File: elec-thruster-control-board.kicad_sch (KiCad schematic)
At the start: 53 parts, among them J1 Conn_01x01, J10 Conn_01x01, J11 gp17-pwm0B, J12 gp2-pwm1A, J14 Conn_01x01, J15 gp6-pwm3A, J16 gp8-pwm4A, J17 Conn_01x01, J18 gp19-pwm1B, J19 gp21-pwm2B, J2 gp0-pwm0A, J20 gp26-pwm5A, J21 gp27-pwm5B, J3 Conn_01x01, J4 Conn_01x01, J5 gp4-pwm2A, J6 Conn_01x01, J7 Conn_01x01, J8 Conn_01x01, J9 Conn_01x01

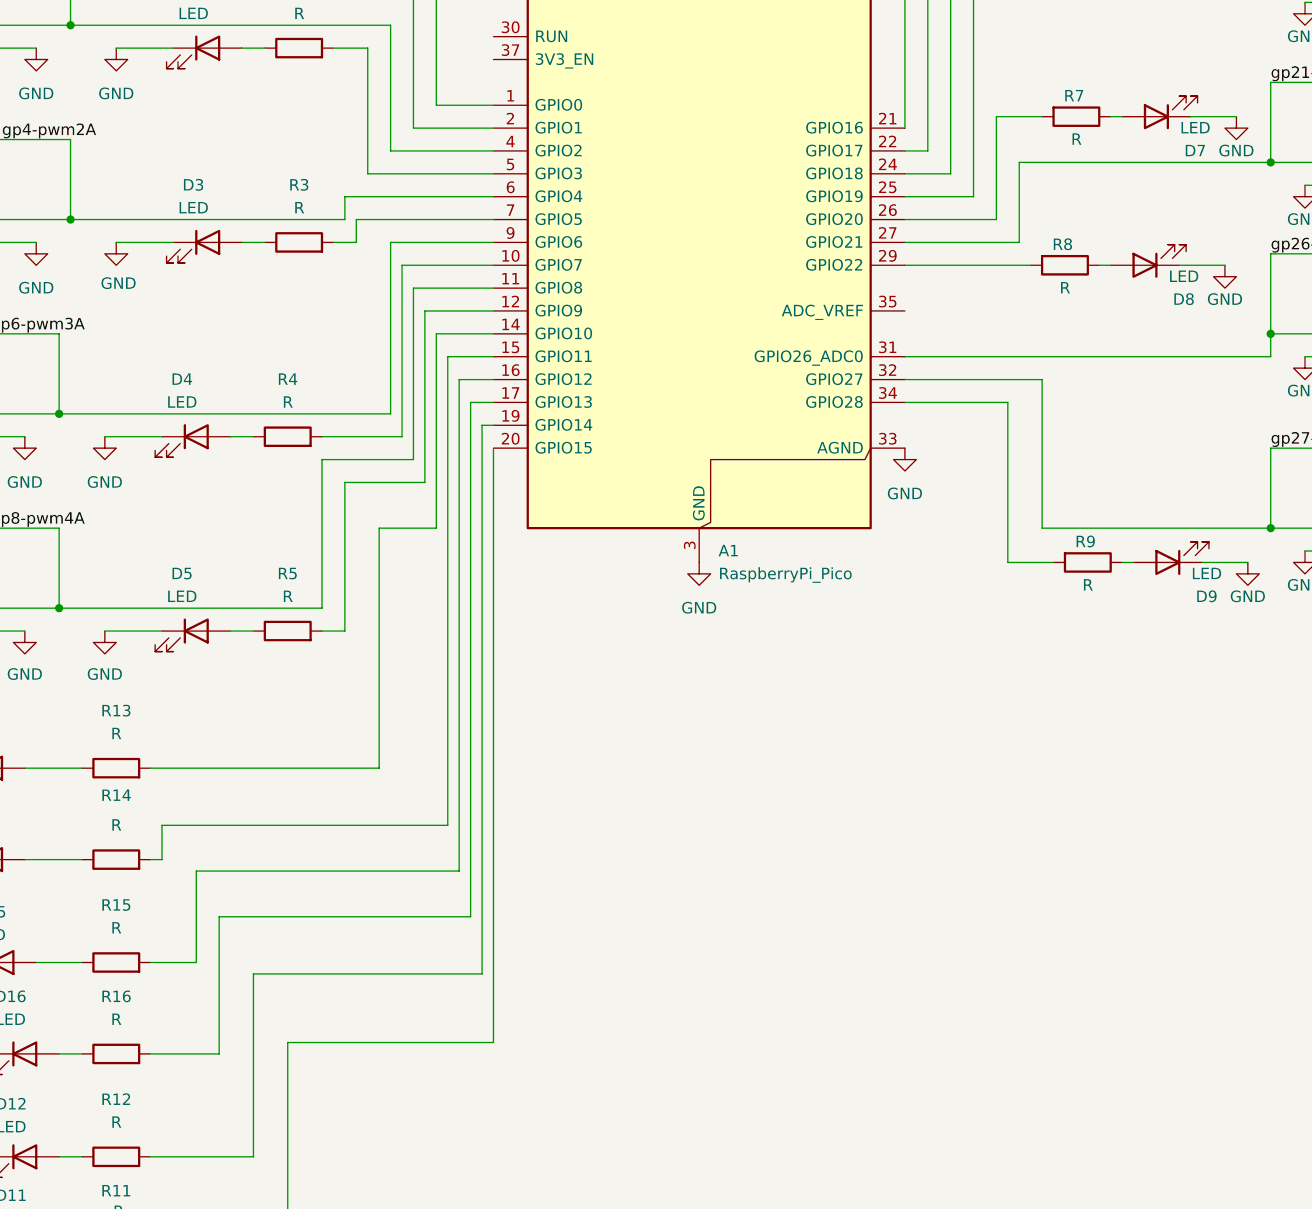
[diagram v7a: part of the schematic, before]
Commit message: Painstakingly added better silkscreening and MOUNTING HOLES!
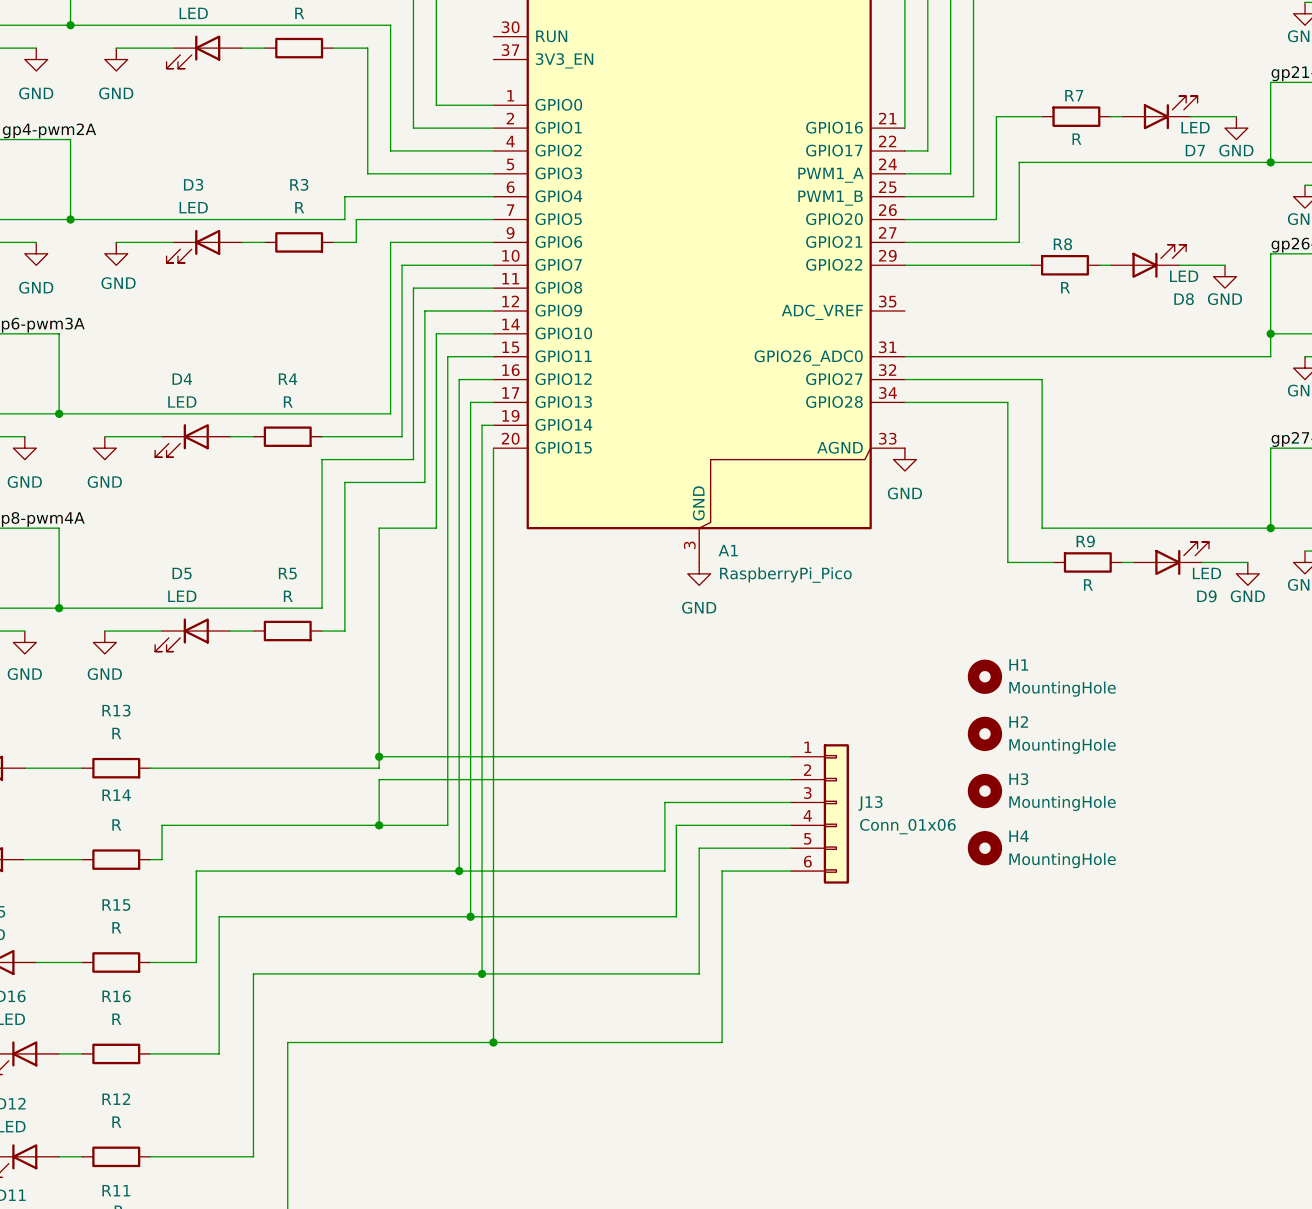
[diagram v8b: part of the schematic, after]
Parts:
- added H1, H2, H3, H4: MountingHole, MountingHole:MountingHole_3.2mm_M3_DIN965_Pad, symbol Mechanical:MountingHole
- added J13: Conn_01x06, Connector_PinHeader_2.54mm:PinHeader_1x06_P2.54mm_Vertical, symbol Connector_Generic:Conn_01x06
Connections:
- net at A1.17 (GPIO13), R16.2: now also J13.4 (Pin_4)
- net at A1.16 (GPIO12), R15.2: now also J13.3 (Pin_3)
- net at A1.14 (GPIO10), R13.2: now also J13.1 (Pin_1)
- net at A1.15 (GPIO11), R14.2: now also J13.2 (Pin_2)
- net at A1.19 (GPIO14), R12.2: now also J13.5 (Pin_5)
- net at A1.20 (GPIO15), R11.2: now also J13.6 (Pin_6)
